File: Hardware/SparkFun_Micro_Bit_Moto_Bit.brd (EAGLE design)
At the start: 58.4 x 76.2 mm, 51 parts, among them J1 POWER_JACKPTH_LOCK, J2 CORTEX_DEBUGPTH, U1 CY8C4245LQI-483, U2 TPS62172, U3 micro:bit, U4 DRV8835

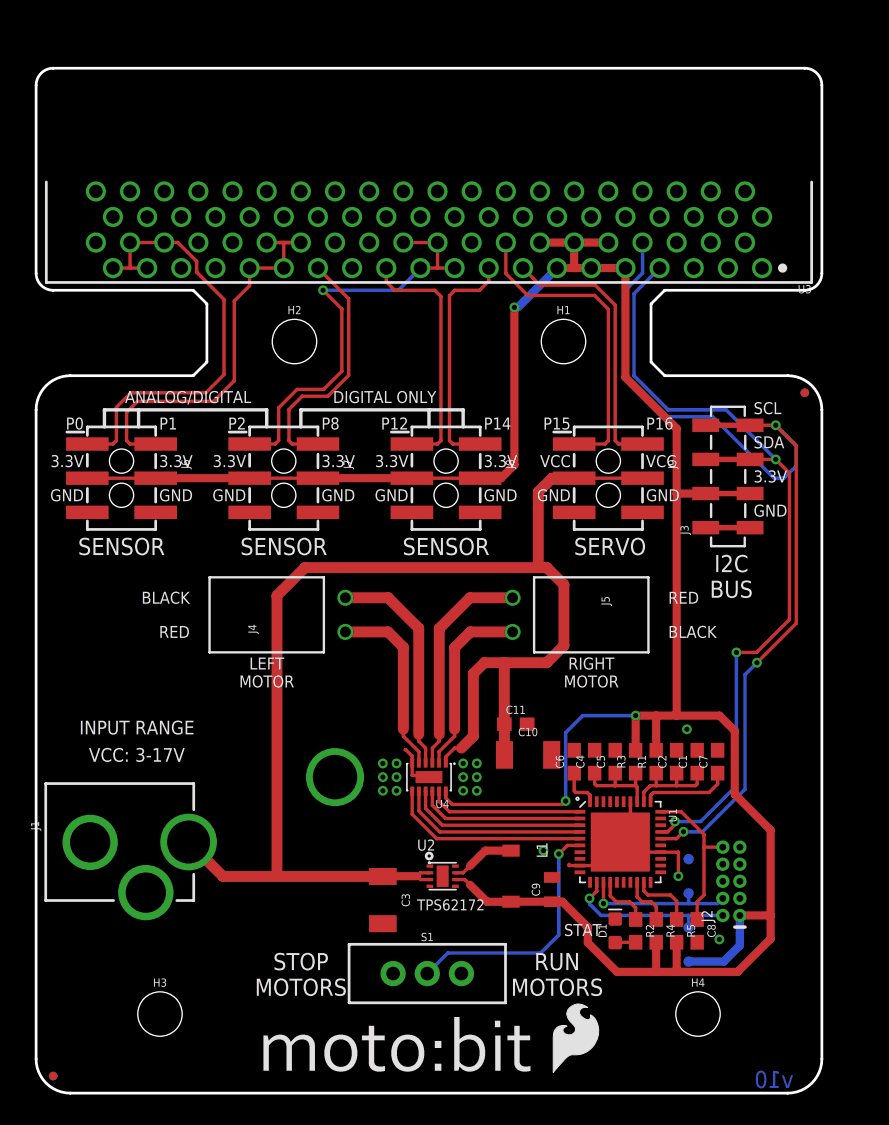
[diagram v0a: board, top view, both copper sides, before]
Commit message: v20
-Updated silk to buzzard text
-Updated the supply range to 11V max
-Replaced 2.2uH inductor of buck regulator
-Added QWIIC Connector
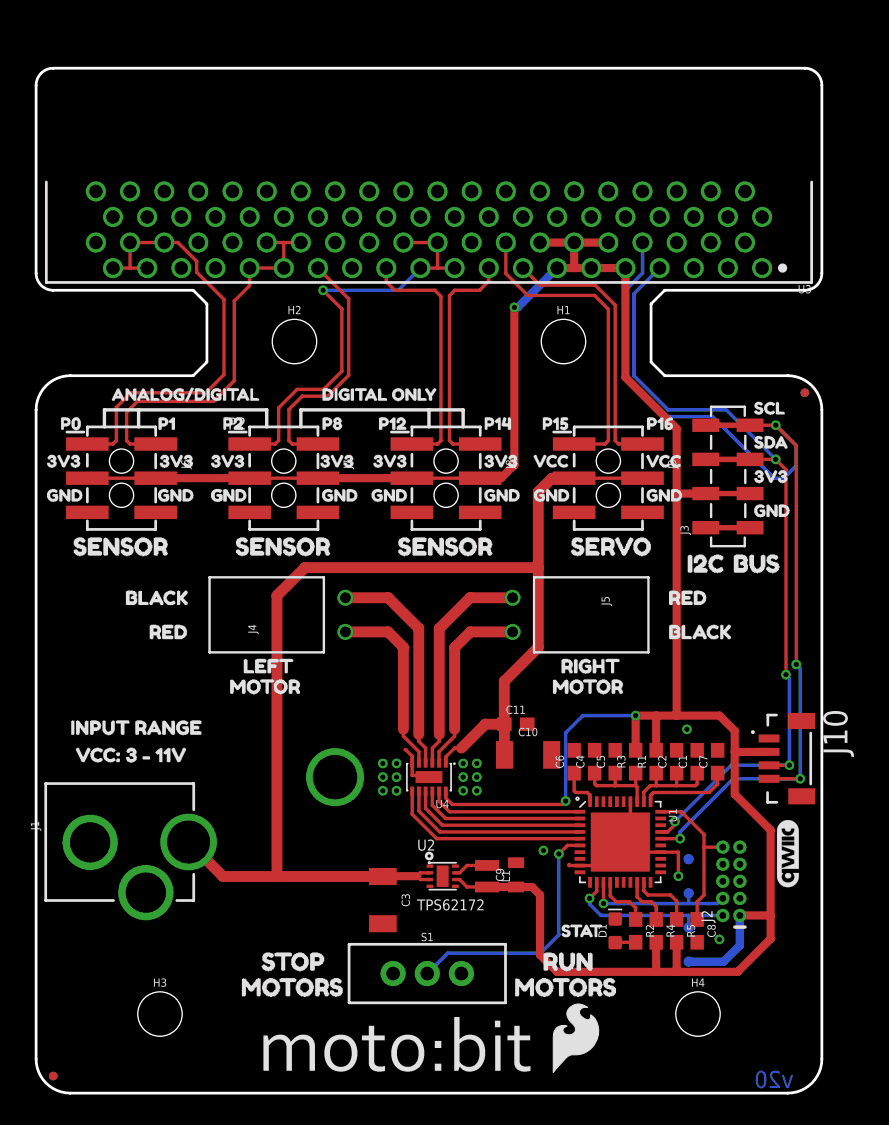
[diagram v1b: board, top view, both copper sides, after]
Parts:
- added J10: (no value), SparkFun-Connectors:JST04_1MM_VERT
- added LOGO3: QWIIC_LOGO_5MM, SparkFun-Aesthetics:QWIIC_5MM
- added U$10, U$13, U$16, U$19, U$22, U$25, U$28, U$32, U$6: (no value), buzzard_labels (17):GND0
- added U$11: (no value), buzzard_labels (17):P24
- added U$12, U$15, U$18, U$21, U$31, U$5, U$9: (no value), buzzard_labels (17):3V31
- added U$14: (no value), buzzard_labels (17):P85
- added U$17: (no value), buzzard_labels (17):P126
- added U$20: (no value), buzzard_labels (17):P147
- added U$23: (no value), buzzard_labels (17):P158
- added U$24, U$27: (no value), buzzard_labels (17):VCC10
- added U$26: (no value), buzzard_labels (17):P169
- added U$29: (no value), buzzard_labels (18):SCL2
- added U$30: (no value), buzzard_labels (18):SDA3
- added U$33: (no value), buzzard_labels (18):I2C4
- added U$34: (no value), buzzard_labels (18):BUS5
- added U$35: (no value), buzzard_labels (18):SERVO6
- added U$36, U$37, U$38: (no value), buzzard_labels (18):SENSOR7
- added U$39: (no value), buzzard_labels (18):ANALOG#DIGITAL0
- added U$40: (no value), buzzard_labels (18):DIGITAL_ONLY1
- added U$41, U$44: (no value), buzzard_labels (18):BLACK8
- added U$42, U$43: (no value), buzzard_labels (18):RED9
- added U$45: (no value), buzzard_labels (18):LEFT10
- added U$46, U$48: (no value), buzzard_labels (18):MOTOR11
- added U$47: (no value), buzzard_labels (18):RIGHT12
- added U$49: (no value), buzzard_labels (18):INPUT_RANGE13
- added U$50: (no value), buzzard_labels (18):VCC#_3_#_11V14
- added U$51: (no value), buzzard_labels (18):STOP15
- added U$52, U$54: (no value), buzzard_labels (18):MOTORS16
- added U$53: (no value), buzzard_labels (18):RUN17
- added U$55: (no value), buzzard_labels (18):STAT18
- added U$7: (no value), buzzard_labels (17):P02
- added U$8: (no value), buzzard_labels (17):P13
- L1: value 2.2µH -> 2.2μH; device SparkFun-Coils:INDUCTOR_2.2UH -> SparkFun-Coils:0805-WIDE
- moved C9 2.88 mm to (35.7, 16.2)
- moved L1 1.78 mm to (33.5, 16.1)
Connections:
- net 3.3V: now also J10.2, L1.2; no longer L1.P$2
- net GND: now also J10.1
- net N$4: now also L1.1; no longer L1.P$1
- net SCL: now also J10.4
- net SDA: now also J10.3
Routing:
- net VCC: track 104.4 -> 95.9 mm
- net SCL: track 72.6 -> 77.4 mm, vias 3 -> 4
- net 3.3V: track 188.6 -> 193.1 mm
- net N$4: track 4.81 -> 2.58 mm
- net SDA: track 58.2 -> 60.3 mm, vias 3 -> 4
- net ANALOG_1: track 30.8 -> 29.2 mm
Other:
- board text added: "v20"
- board text removed: "3.3V"
- board text removed: "ANALOG/DIGITAL"
- board text removed: "BLACK"
- board text removed: "DIGITAL ONLY"
- board text removed: "I2C BUS"
- board text removed: "INPUT RANGE"
- board text removed: "LEFT MOTOR"
- board text removed: "P0"
- board text removed: "P1"
- board text removed: "P12"
- board text removed: "P14"
- board text removed: "P15"
- board text removed: "P16"
- board text removed: "P8"
- board text removed: "RED"
- board text removed: "RIGHT MOTOR"
- board text removed: "RUN MOTORS"
- board text removed: "SCL"
- board text removed: "SDA"
- board text removed: "SENSOR"
- board text removed: "SERVO"
- board text removed: "STAT"
- board text removed: "STOP MOTORS"
- board text removed: "VCC"
- board text removed: "VCC: 3-17V"
- board text removed: "v10"

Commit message: Design Review Changes
pushed a couple traces to get better ground pour coverage.
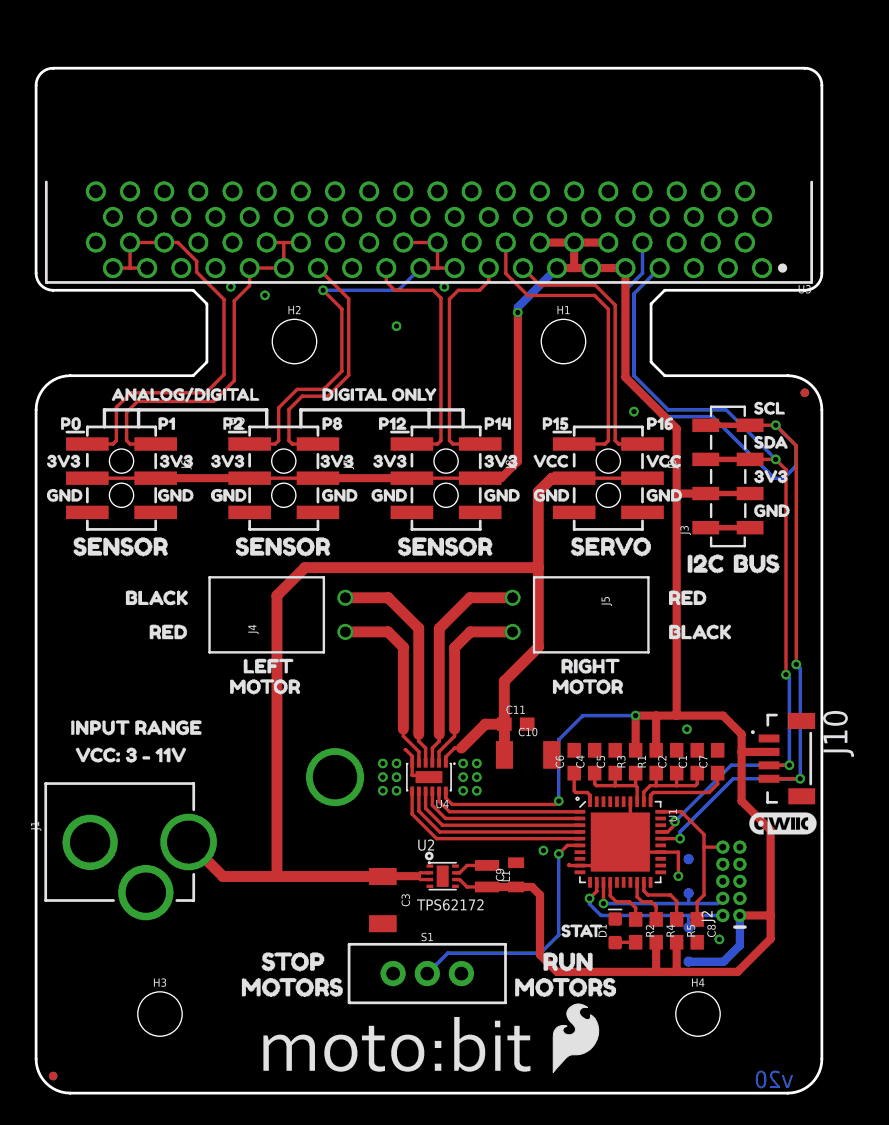
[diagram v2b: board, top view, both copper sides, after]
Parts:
- moved LOGO3 2.32 mm to (55.5, 20.1), turned to 0 degrees
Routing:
- net 3.3V: track 193.1 -> 192.3 mm
- net GND: vias 17 -> 22
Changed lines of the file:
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@@
 <layer number="45" name="Holes" color="7" fill="1" visible="yes" active="yes"/>
 <layer number="46" name="Milling" color="3" fill="1" visible="no" active="yes"/>
-<layer number="47" name="Measures" color="7" fill="1" visible="no" active="yes"/>
+<layer number="47" name="Measures" color="7" fill="1" visible="yes" active="yes"/>
 <layer number="48" name="Document" color="7" fill="1" visible="no" active="yes"/>
 <layer number="49" name="Reference" color="7" fill="1" visible="no" active="yes"/>
@@
 <attribute name="VALUE" x="50.90066875" y="28.559" size="1.778" layer="27" rot="R270"/>
 </element>
-<element name="LOGO3" library="SparkFun-Aesthetics" package="QWIIC_5MM" value="QWIIC_LOGO_5MM" x="55.88" y="17.78" smashed="yes" rot="R90"/>
+<element name="LOGO3" library="SparkFun-Aesthetics" package="QWIIC_5MM" value="QWIIC_LOGO_5MM" x="55.499" y="20.066" smashed="yes"/>
 </elements>
 <signals>
@@
 <via x="22.225" y="23.495" extent="1-16" drill="3.302"/>
 <contactref element="J10" pad="1"/>
+<via x="26.797" y="57.023" extent="1-16" drill="0.381"/>
+<via x="17.018" y="59.309" extent="1-16" drill="0.381"/>
+<via x="14.478" y="59.944" extent="1-16" drill="0.381"/>
+<via x="30.353" y="59.944" extent="1-16" drill="0.381"/>
+<via x="44.45" y="50.673" extent="1-16" drill="0.381"/>
 </signal>
 <signal name="3.3V">
@@
 <wire x1="8.89" y1="45.72" x2="15.875" y2="45.72" width="0.6096" layer="1"/>
 <wire x1="20.955" y1="45.72" x2="27.94" y2="45.72" width="0.6096" layer="1"/>
-<via x="35.56" y="58.42" extent="1-16" drill="0.381"/>
+<via x="35.814" y="58.039" extent="1-16" drill="0.381"/>
 <wire x1="49.785" y1="44.577" x2="47.625" y2="44.577" width="0.6096" layer="1"/>
 <wire x1="47.625" y1="44.577" x2="47.625" y2="49.408071875" width="0.6096" layer="1"/>
@@
 <wire x1="51.1258875" y1="9.779" x2="52.324" y2="10.9771125" width="0.6096" layer="16"/>
 <wire x1="52.324" y1="10.9771125" x2="52.324" y2="13.208" width="0.6096" layer="16"/>
-<wire x1="47.625" y1="28.067" x2="50.8136625" y2="28.067" width="0.6096" layer="1"/>
+<wire x1="47.625" y1="28.067" x2="51.0676625" y2="28.067" width="0.6096" layer="1"/>
 <wire x1="47.625" y1="28.067" x2="46.101" y2="28.067" width="0.6096" layer="1"/>
 <wire x1="46.101" y1="28.067" x2="46.101" y2="25.488" width="0.6096" layer="1"/>
@@
 <wire x1="30.46" y1="22.445" x2="30.46" y2="21.937675" width="0.254" layer="1"/>
 <wire x1="30.46" y1="21.937675" x2="30.934675" y2="21.463" width="0.254" layer="1"/>
-<wire x1="30.934675" y1="21.463" x2="39.116" y2="21.463" width="0.254" layer="1"/>
-<wire x1="35.56" y1="58.42" x2="35.56" y2="46.7119" width="0.6096" layer="1"/>
-<wire x1="35.56" y1="46.7119" x2="34.5681" y2="45.72" width="0.6096" layer="1"/>
+<wire x1="30.934675" y1="21.463" x2="38.608" y2="21.463" width="0.254" layer="1"/>
+<wire x1="35.814" y1="58.039" x2="35.814" y2="46.9659" width="0.6096" layer="1"/>
+<wire x1="35.814" y1="46.9659" x2="34.5681" y2="45.72" width="0.6096" layer="1"/>
 <wire x1="34.5681" y1="45.72" x2="33.02" y2="45.72" width="0.6096" layer="1"/>
-<via x="39.37" y="21.717" extent="1-16" drill="0.381"/>
+<via x="38.862" y="21.717" extent="1-16" drill="0.381"/>
 <wire x1="54.61" y1="19.558" x2="54.61" y2="13.208" width="0.6096" layer="1"/>
 <wire x1="54.61" y1="13.208" x2="54.61" y2="11.469" width="0.6096" layer="1"/>
-<wire x1="39.37" y1="21.717" x2="39.37" y2="26.79066875" width="0.254" layer="16"/>
-<wire x1="39.37" y1="26.79066875" x2="40.64633125" y2="28.067" width="0.254" layer="16"/>
+<wire x1="38.862" y1="21.717" x2="38.862" y2="26.28266875" width="0.254" layer="16"/>
+<wire x1="38.862" y1="26.28266875" x2="40.64633125" y2="28.067" width="0.254" layer="16"/>
 <wire x1="40.64633125" y1="28.067" x2="44.577" y2="28.067" width="0.254" layer="16"/>
 <via x="44.577" y="28.067" extent="1-16" drill="0.381"/>
 <wire x1="52.324" y1="13.208" x2="54.61" y2="13.208" width="0.6096" layer="1"/>
-<wire x1="54.61" y1="19.558" x2="51.943" y2="22.225" width="0.6096" layer="1"/>
-<wire x1="51.943" y1="22.225" x2="51.943" y2="25.37" width="0.6096" layer="1"/>
-<wire x1="51.943" y1="25.37" x2="51.943" y2="26.9376625" width="0.6096" layer="1"/>
-<wire x1="51.943" y1="26.9376625" x2="50.8136625" y2="28.067" width="0.6096" layer="1"/>
+<wire x1="54.61" y1="19.558" x2="52.451" y2="21.717" width="0.6096" layer="1"/>
+<wire x1="52.451" y1="21.717" x2="52.451" y2="25.37" width="0.6096" layer="1"/>
+<wire x1="52.451" y1="25.37" x2="52.451" y2="26.6836625" width="0.6096" layer="1"/>
+<wire x1="52.451" y1="26.6836625" x2="51.0676625" y2="28.067" width="0.6096" layer="1"/>
 <wire x1="47.625" y1="9.017" x2="52.158" y2="9.017" width="0.6096" layer="1"/>
 <wire x1="52.158" y1="9.017" x2="54.61" y2="11.469" width="0.6096" layer="1"/>
@@
 <wire x1="46.101" y1="11.215" x2="46.101" y2="9.017" width="0.6096" layer="1"/>
 <wire x1="46.101" y1="9.017" x2="47.625" y2="9.017" width="0.6096" layer="1"/>
-<wire x1="35.56" y1="58.42" x2="35.814" y2="58.42" width="0.6096" layer="16"/>
+<wire x1="35.814" y1="58.039" x2="35.814" y2="58.42" width="0.6096" layer="16"/>
 <wire x1="35.814" y1="58.42" x2="38.735" y2="61.341" width="0.6096" layer="16"/>
-<wire x1="39.116" y1="21.463" x2="39.37" y2="21.717" width="0.254" layer="1"/>
+<wire x1="38.608" y1="21.463" x2="38.862" y2="21.717" width="0.254" layer="1"/>
 <wire x1="35.687" y1="15.3306" x2="36.870628125" y2="15.3306" width="0.6096" layer="1"/>
 <wire x1="27.94" y1="45.72" x2="33.02" y2="45.72" width="0.254" layer="1"/>
@@
 <wire x1="38.735" y1="9.017" x2="46.101" y2="9.017" width="0.6096" layer="1"/>
 <contactref element="J10" pad="2"/>
-<wire x1="54.496" y1="25.37" x2="51.943" y2="25.37" width="0.6096" layer="1"/>
+<wire x1="54.496" y1="25.37" x2="52.451" y2="25.37" width="0.6096" layer="1"/>
 </signal>
 <signal name="SDA">
@@
 <wire x1="27.94" y1="48.26" x2="29.845" y2="48.26" width="0.254" layer="1"/>
 <wire x1="29.845" y1="48.26" x2="30.099" y2="48.514" width="0.254" layer="1"/>
-<wire x1="30.099" y1="48.514" x2="30.099" y2="59.232096875" width="0.254" layer="1"/>
-<wire x1="30.099" y1="59.232096875" x2="29.641096875" y2="59.69" width="0.254" layer="1"/>
-<wire x1="29.641096875" y1="59.69" x2="26.67" y2="59.69" width="0.254" layer="1"/>
+<wire x1="30.099" y1="48.514" x2="30.099" y2="59.105096875" width="0.254" layer="1"/>
+<wire x1="30.099" y1="59.105096875" x2="29.514096875" y2="59.69" width="0.254" layer="1"/>
+<wire x1="29.514096875" y1="59.69" x2="26.67" y2="59.69" width="0.254" layer="1"/>
 <wire x1="26.67" y1="59.69" x2="26.035" y2="60.325" width="0.254" layer="1"/>
 <wire x1="26.035" y1="60.325" x2="26.035" y2="61.341" width="0.254" layer="1"/>
@@
 <wire x1="33.02" y1="48.26" x2="30.988" y2="48.26" width="0.254" layer="1"/>
 <wire x1="30.988" y1="48.26" x2="30.734" y2="48.514" width="0.254" layer="1"/>
-<wire x1="30.734" y1="48.514" x2="30.734" y2="59.28839375" width="0.254" layer="1"/>
-<wire x1="30.734" y1="59.28839375" x2="31.13560625" y2="59.69" width="0.254" layer="1"/>
+<wire x1="30.734" y1="48.514" x2="30.734" y2="59.03439375" width="0.254" layer="1"/>
+<wire x1="30.734" y1="59.03439375" x2="31.38960625" y2="59.69" width="0.254" layer="1"/>
 <wire x1="33.655" y1="61.341" x2="33.655" y2="60.373915625" width="0.254" layer="1"/>
 <wire x1="33.655" y1="60.373915625" x2="32.971084375" y2="59.69" width="0.254" layer="1"/>
-<wire x1="32.971084375" y1="59.69" x2="31.13560625" y2="59.69" width="0.254" layer="1"/>
+<wire x1="32.971084375" y1="59.69" x2="31.38960625" y2="59.69" width="0.254" layer="1"/>
 </signal>
 <signal name="SERVO_16">
